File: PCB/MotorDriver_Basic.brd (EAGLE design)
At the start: 27.1 x 36.8 mm, 17 parts, among them IC1 MPU6050, U1 DRV8835

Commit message: Tweaked the board file
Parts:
- moved JP2 67.4 mm to (12.7, 2.54)
- moved C7 50.2 mm to (5.08, 17.8), turned to 0 degrees
- moved R5 46.0 mm to (5.08, 24.1), turned to 0 degrees
- moved C2 45.0 mm to (10.2, 8.89), turned to 90 degrees
- moved C5 41.9 mm to (6.35, 8.89), turned to 90 degrees
- moved U$2 41.0 mm to (20.3, 16.5), turned to 90 degrees
- moved C1 37.2 mm to (14.0, 8.89), turned to 90 degrees
- moved C6 36.1 mm to (19.1, 8.89)
- moved C4 33.0 mm to (12.7, 17.8)
- moved IC1 30.7 mm to (12.7, 25.4), turned to 90 degrees
- moved U1 26.9 mm to (5.08, 30.5), turned to 180 degrees
- moved C3 26.7 mm to (20.3, 24.1)
- moved R1 24.3 mm to (20.3, 40.6), turned to 0 degrees
- moved R2 24.2 mm to (15.2, 40.6), turned to 0 degrees
- moved R4 24.2 mm to (5.08, 40.6), turned to 0 degrees
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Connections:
- net AIN1: now also JP2.4; no longer JP2.1
- net AIN2: now also JP2.3; no longer JP2.2
- net BIN1: now also JP2.2; no longer JP2.3
- net BIN2: now also JP2.1; no longer JP2.4
- net GND: now also JP1.5, JP2.5, JP2.6; no longer JP1.1, JP1.2, JP1.4
- net IMU_INT: now also JP1.8; no longer JP1.3
- net MOUTA1: now also JP1.4; no longer JP2.8
- net MOUTA2: now also JP1.3; no longer JP2.7
- net MOUTB1: now also JP1.2; no longer JP1.8
- net MOUTB2: now also JP1.1; no longer JP1.7
- net SCL: now also JP2.7; no longer JP1.6
- net SDA: now also JP2.8; no longer JP1.5
- net VCC: now also JP1.7; no longer JP2.6
- net VM: now also JP1.6; no longer JP2.5
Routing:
- net VM: track 79.2 -> 0.00 mm, vias 2 -> 0
- net VCC: track 62.2 -> 0.00 mm
- net SDA: track 53.5 -> 0.00 mm, vias 4 -> 0
- net IMU_INT: track 41.5 -> 0.00 mm, vias 2 -> 0
- net SCL: track 39.4 -> 0.00 mm, vias 2 -> 0
- net MOUTB1: track 38.9 -> 0.00 mm
- net MOUTA2: track 37.4 -> 0.00 mm, vias 1 -> 0
- net MOUTA1: track 30.8 -> 0.00 mm, vias 1 -> 0
- net MOUTB2: track 28.5 -> 0.00 mm, vias 1 -> 0
- net O.S.: track 16.0 -> 0.00 mm
- net BIN2: track 14.0 -> 0.00 mm, vias 1 -> 0
- net BIN1: track 13.1 -> 0.00 mm, vias 1 -> 0
- net AIN1: track 12.4 -> 0.00 mm, vias 1 -> 0
- net AIN2: track 12.2 -> 0.00 mm, vias 1 -> 0
- net N$2: track 10.8 -> 0.00 mm, vias 2 -> 0
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- removed copper zone on layer 1, net GND
- removed copper zone on layer 16, net GND
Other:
- board size 27.1 x 36.8 mm -> 25.4 x 50.8 mm

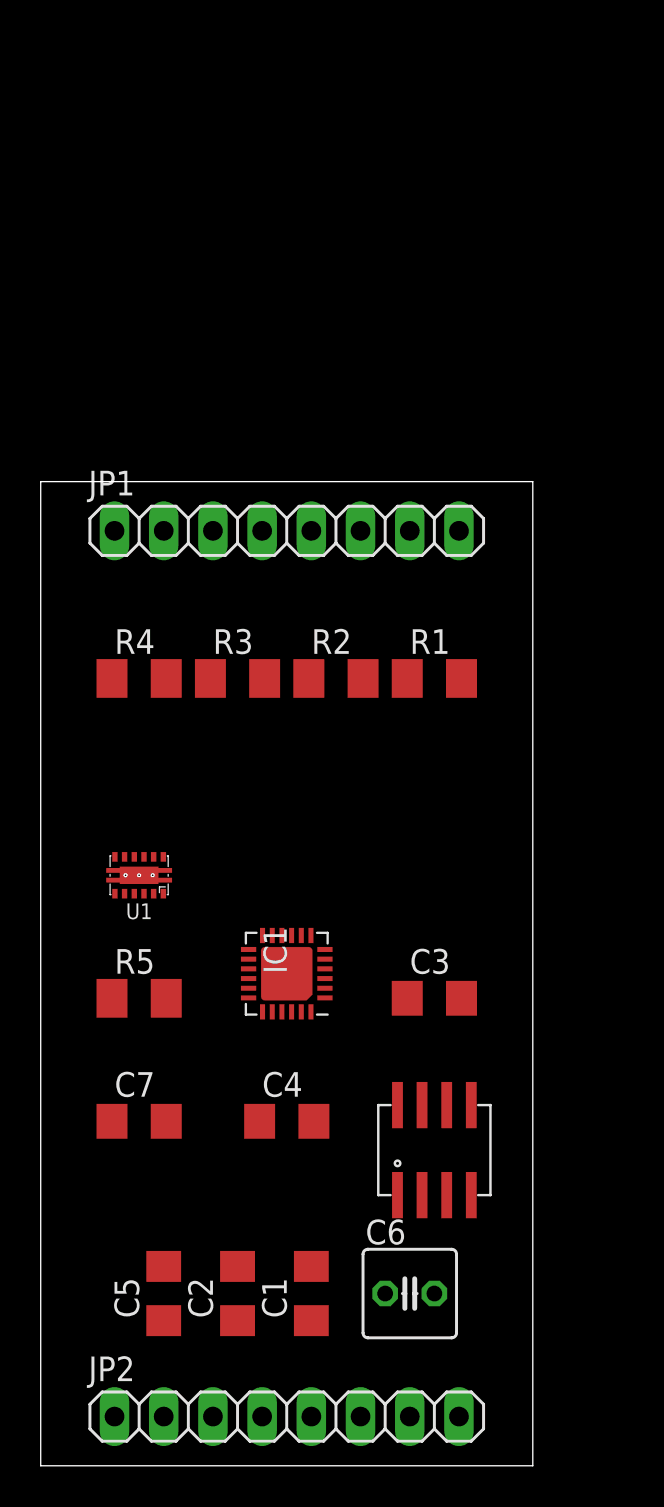
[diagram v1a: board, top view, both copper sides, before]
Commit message: Added some connections
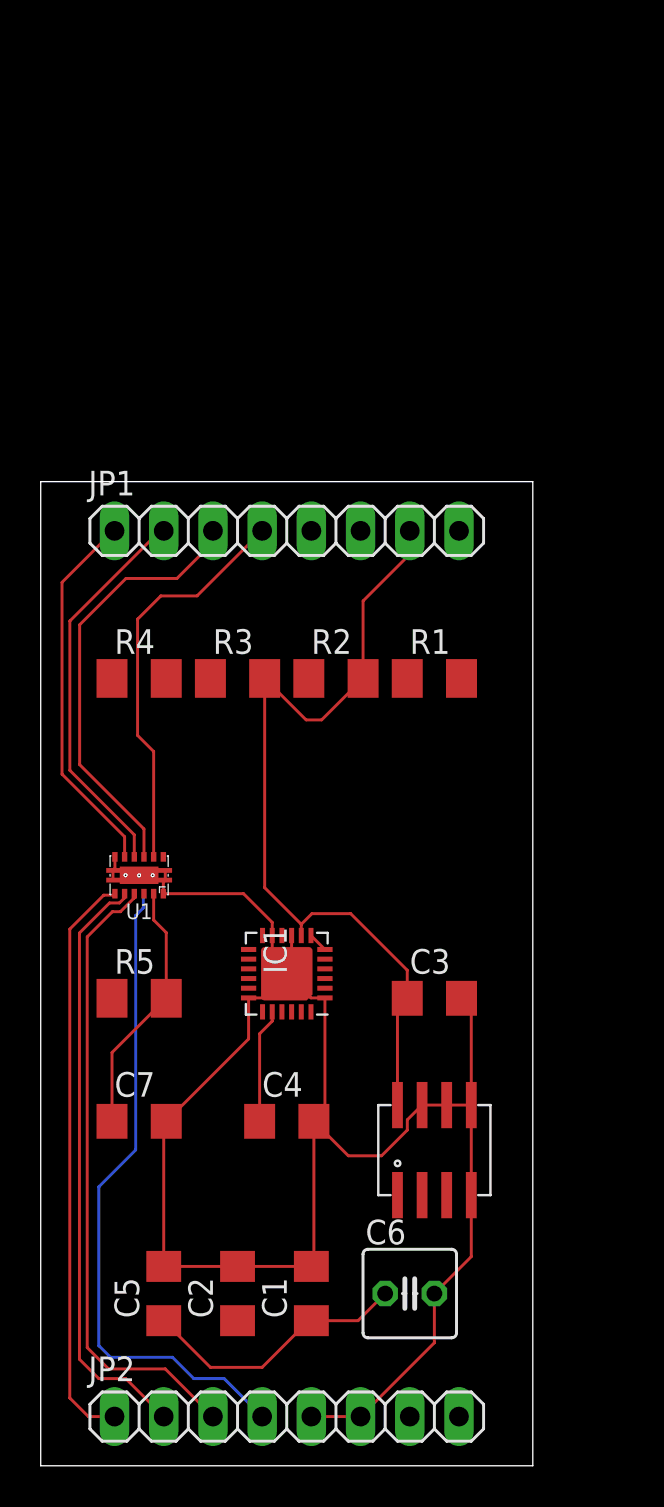
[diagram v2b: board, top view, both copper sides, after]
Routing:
- net GND: track 0.00 -> 94.2 mm
- net VCC: track 0.00 -> 56.8 mm
- net AIN1: track 0.00 -> 34.0 mm
- net AIN2: track 0.00 -> 32.6 mm
- net BIN1: track 0.00 -> 30.9 mm
- net BIN2: track 0.00 -> 30.0 mm
- net MOUTA2: track 0.00 -> 22.6 mm
- net MOUTA1: track 0.00 -> 20.9 mm
- net MOUTB1: track 0.00 -> 20.3 mm
- net MOUTB2: track 0.00 -> 19.3 mm
- net VM: track 0.00 -> 14.0 mm
- net N$1: track 0.00 -> 5.92 mm

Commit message: Tweaked schematic/Created board
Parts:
- removed R1: 0, rcl:M1206
- removed R2: 10K, rcl:M1206
- R4, R5: value 10K -> 3.3K
- moved R4 31.9 mm to (11.7, 9.40), turned to 180 degrees
- moved C1 27.3 mm to (8.13, 35.6), turned to 180 degrees
- moved C5 26.0 mm to (16.0, 33.0)
- moved C6 25.0 mm to (7.87, 31.2), turned to 90 degrees
- moved C2 24.3 mm to (13.0, 33.0)
- moved C7 20.7 mm to (19.1, 33.0), turned to 90 degrees
- moved R3 14.8 mm to (23.1, 33.5), turned to 90 degrees
- moved C3 13.4 mm to (7.37, 20.6), turned to 270 degrees
- moved R5 12.5 mm to (11.7, 13.5), turned to 180 degrees
- moved U$2 9.16 mm to (20.8, 25.7)
- moved U1 5.33 mm to (5.08, 25.1)
- moved C4 1.48 mm to (11.9, 19.1), turned to 270 degrees
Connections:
- removed net N$2: IC1.12, R1.1
- net IMU_INT: now also IC1.12; no longer R1.2, R2.1
- net VCC: now also C5.1, IC1.13; no longer R2.2
- net VM: no longer C5.1, IC1.13
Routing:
- net GND: track 94.2 -> 12.0 mm
- net SCL: track 0.00 -> 39.3 mm, vias 0 -> 2
- net SDA: track 0.00 -> 35.4 mm
- net IMU_INT: track 0.00 -> 25.1 mm, vias 0 -> 1
- net VM: track 14.0 -> 28.3 mm
- net AIN1: track 34.0 -> 24.2 mm
- net O.S.: track 0.00 -> 9.70 mm, vias 0 -> 2
- net AIN2: track 32.6 -> 23.3 mm
- net BIN1: track 30.9 -> 22.5 mm
- net BIN2: track 30.0 -> 21.7 mm
- net VCC: track 56.8 -> 63.4 mm
- net MOUTB2: track 19.3 -> 24.3 mm
- net MOUTA1: track 20.9 -> 25.5 mm
- net REGOUT: track 0.00 -> 4.46 mm, vias 0 -> 2
- net MOUTB1: track 20.3 -> 24.7 mm
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- added copper zone on layer 1, net GND
- added copper zone on layer 16, net GND
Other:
- board text added: "AIN1"
- board text added: "AIN2"
- board text added: "AO1"
- board text added: "AO2"
- board text added: "BIN1"
- board text added: "BIN2"
- board text added: "BO1"
- board text added: "BO2"
- board text added: "ECE 5780 Low-voltage Motor Driver PCB Prototype V1.0"
- board text added: "Forward >"
- board text added: "GND"
- board text added: "INT"
- board text added: "SCL"
- board text added: "SDA"
- board text added: "VCC"
- board text added: "VM"

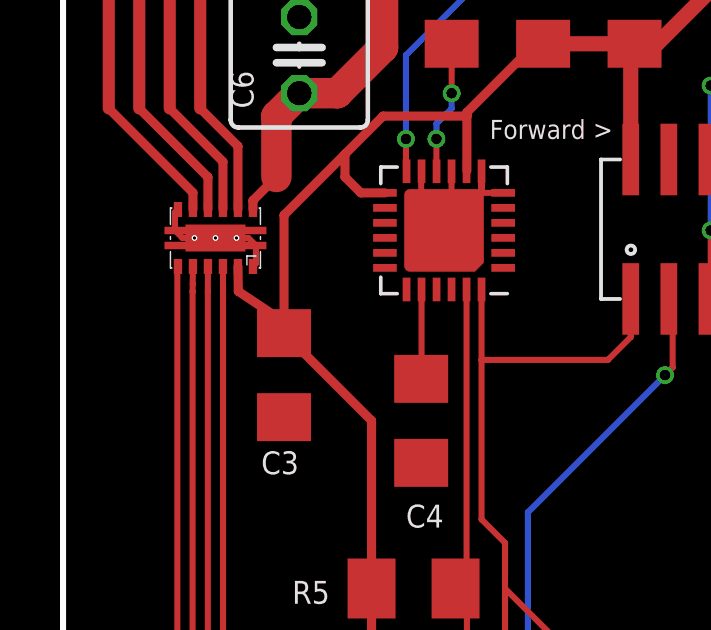
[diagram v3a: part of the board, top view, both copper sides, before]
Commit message: Fixed the fucking asshole's mistake where the fuck did we get that fucking foot print fuck fuck fuck fuck fuck
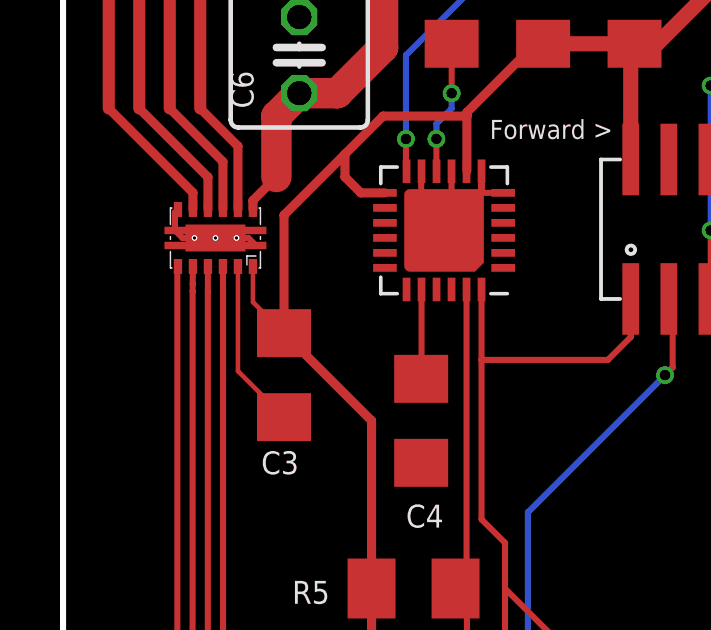
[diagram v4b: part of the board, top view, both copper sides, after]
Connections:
- net GND: now also U1.11; no longer U1.12
- net VCC: now also U1.12; no longer U1.11
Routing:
- net GND: track 12.0 -> 16.9 mm
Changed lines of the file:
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@@
 <?xml version="1.0" encoding="utf-8"?>
 <!DOCTYPE eagle SYSTEM "eagle.dtd">
-<eagle version="9.2.2">
+<eagle version="9.3.2">
 <drawing>
 <settings>
@@
 <setting verticaltext="up"/>
 </settings>
-<grid distance="10" unitdist="mil" unit="mil" style="lines" multiple="1" display="no" altdistance="5" altunitdist="mil" altunit="mil"/>
+<grid distance="0.1" unitdist="mil" unit="mil" style="lines" multiple="1" display="no" altdistance="5" altunitdist="mil" altunit="mil"/>
 <layers>
 <layer number="1" name="Top" color="4" fill="1" visible="yes" active="yes"/>
@@
 <contactref element="U1" pad="PAD"/>
 <contactref element="U1" pad="6"/>
-<contactref element="U1" pad="12"/>
+<contactref element="U1" pad="11"/>
 <contactref element="IC1" pad="1"/>
 <contactref element="IC1" pad="6"/>
@@
 <wire x1="11.938" y1="27.358" x2="11.938" y2="26.67" width="0.2032" layer="1"/>
 <wire x1="12.7" y1="25.908" x2="11.938" y2="26.67" width="0.2032" layer="1"/>
-<wire x1="6.33" y1="24.196" x2="6.43" y2="24.296" width="0.2032" layer="1"/>
-<wire x1="6.43" y1="24.296" x2="6.43" y2="24.896" width="0.2032" layer="1"/>
 <wire x1="3.83" y1="26.096" x2="3.73" y2="25.996" width="0.2032" layer="1"/>
 <wire x1="3.73" y1="25.996" x2="3.73" y2="25.396" width="0.2032" layer="1"/>
@@
 <wire x1="12.7" y1="25.658" x2="12.95" y2="25.908" width="0.2032" layer="1"/>
 <wire x1="12.7" y1="25.4" x2="12.7" y2="25.908" width="0.2032" layer="1"/>
+<wire x1="5.83" y1="24.196" x2="5.83" y2="20.71" width="0.1524" layer="1"/>
+<wire x1="5.83" y1="20.71" x2="7.366" y2="19.174" width="0.1524" layer="1"/>
 </signal>
 <signal name="SDA">
@@
 </signal>
 <signal name="VCC">
-<contactref element="U1" pad="11"/>
+<contactref element="U1" pad="12"/>
 <contactref element="C3" pad="1"/>
 <contactref element="R5" pad="2"/>
@@
 <wire x1="9.398" y1="27.178" x2="9.926" y2="26.65" width="0.3048" layer="1"/>
 <wire x1="9.398" y1="27.94" x2="7.366" y2="25.908" width="0.3048" layer="1"/>
-<wire x1="7.366" y1="21.844" x2="7.366" y2="22.352" width="0.3048" layer="1"/>
-<wire x1="7.366" y1="22.352" x2="7.366" y2="25.908" width="0.3048" layer="1"/>
+<wire x1="7.366" y1="21.844" x2="7.366" y2="25.908" width="0.3048" layer="1"/>
 <wire x1="23.114" y1="34.928" x2="19.806" y2="31.62" width="0.508" layer="1"/>
 <wire x1="19.806" y1="31.62" x2="19.05" y2="31.62" width="0.508" layer="1"/>
-<wire x1="5.83" y1="24.196" x2="5.842" y2="23.368" width="0.3048" layer="1"/>
-<wire x1="5.842" y1="23.368" x2="7.366" y2="22.352" width="0.3048" layer="1"/>
 <wire x1="7.366" y1="21.974" x2="10.284" y2="19.056" width="0.3048" layer="1"/>
 <wire x1="10.284" y1="19.056" x2="10.284" y2="13.462" width="0.3048" layer="1"/>
 <wire x1="10.284" y1="13.462" x2="10.284" y2="9.398" width="0.3048" layer="1"/>
 <wire x1="7.366" y1="21.974" x2="7.366" y2="21.844" width="0.508" layer="1"/>
+<wire x1="7.366" y1="21.974" x2="6.33" y2="23.01" width="0.1524" layer="1"/>
+<wire x1="6.33" y1="23.01" x2="6.33" y2="24.196" width="0.1524" layer="1"/>
 </signal>
 <signal name="VM">
